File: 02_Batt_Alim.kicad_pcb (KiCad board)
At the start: 2 copper layers, 58.4 x 26.7 mm, 52 parts, among them IC1 TP4056, IC2 DW01A, J1 Conn_01x01, J10 Conn_01x01, J11 Conn_01x01, J12 Conn_01x01, J2 Conn_01x01, J3 Conn_01x01, J4 Conn_01x01, J5 Conn_01x01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

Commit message: routage
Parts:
- moved J3 55.8 mm to (104.1, 94.0), turned to 180 degrees
- moved J4 53.4 mm to (104.1, 91.4), turned to 180 degrees
- moved J5 51.4 mm to (104.1, 88.9), turned to 180 degrees
- moved J6 49.9 mm to (104.1, 86.4), turned to 180 degrees
- moved J7 48.9 mm to (104.1, 83.8), turned to 180 degrees
- moved J8 48.3 mm to (104.1, 81.3), turned to 180 degrees
- moved C3 46.5 mm to (108.0, 92.1), turned to 90 degrees
- moved R1 43.3 mm to (107.3, 87.6), turned to 90 degrees
- moved D5 41.4 mm to (113.0, 90.8), turned to 0 degrees
- moved U1 41.3 mm to (113.0, 94.0), turned to 180 degrees
- moved Q2 39.8 mm to (109.9, 87.0), turned to 180 degrees
- moved R15 38.4 mm to (130.8, 94.0)
- moved D6 37.1 mm to (127.2, 94.0), turned to 180 degrees
- moved R5 36.5 mm to (113.2, 86.4), turned to 180 degrees
- moved R2 35.2 mm to (113.2, 88.3), turned to 0 degrees
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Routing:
- net V_OUT: track 69.9 -> 35.5 mm
- net SWITCH_OUT: track 54.0 -> 27.5 mm, vias 0 -> 1
- net uC_2_V: track 34.4 -> 10.5 mm, vias 1 -> 0
- net GND: track 215.9 -> 235.8 mm, vias 31 -> 30
- net Net-(Q1-Pad4): track 4.02 -> 21.5 mm, vias 0 -> 2
- net 5V: track 19.6 -> 36.9 mm, vias 0 -> 2
- net V_BAT-: track 31.1 -> 25.0 mm, vias 1 -> 2
- net /LX: track 14.2 -> 18.1 mm
- net V_BAT+: track 46.6 -> 43.5 mm
- net V_2_uC: track 13.3 -> 10.4 mm
- net SWITCH_IN: track 67.7 -> 70.1 mm, vias 0 -> 2
- net /V_BAT+_F: track 7.08 -> 4.73 mm
- net Net-(IC2-Pad2): track 2.23 -> 3.87 mm
- net Net-(IC2-Pad1): track 11.4 -> 10.0 mm
- net Net-(IC2-Pad3): track 12.7 -> 11.5 mm, vias 2 -> 0
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- added copper zone on B.Cu, net V_BAT-
- removed copper zone on F.Cu, net /V_BAT+_F
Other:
- board size 58.4 x 26.7 mm -> 34.3 x 43.2 mm
- board text added: "Batt_Alim 2020/12/22"
- board text added: "https://github.com/ThierryOrlandi/02_Batt_Alim"
- board text removed: "Batt_Alim 2020/12/15"

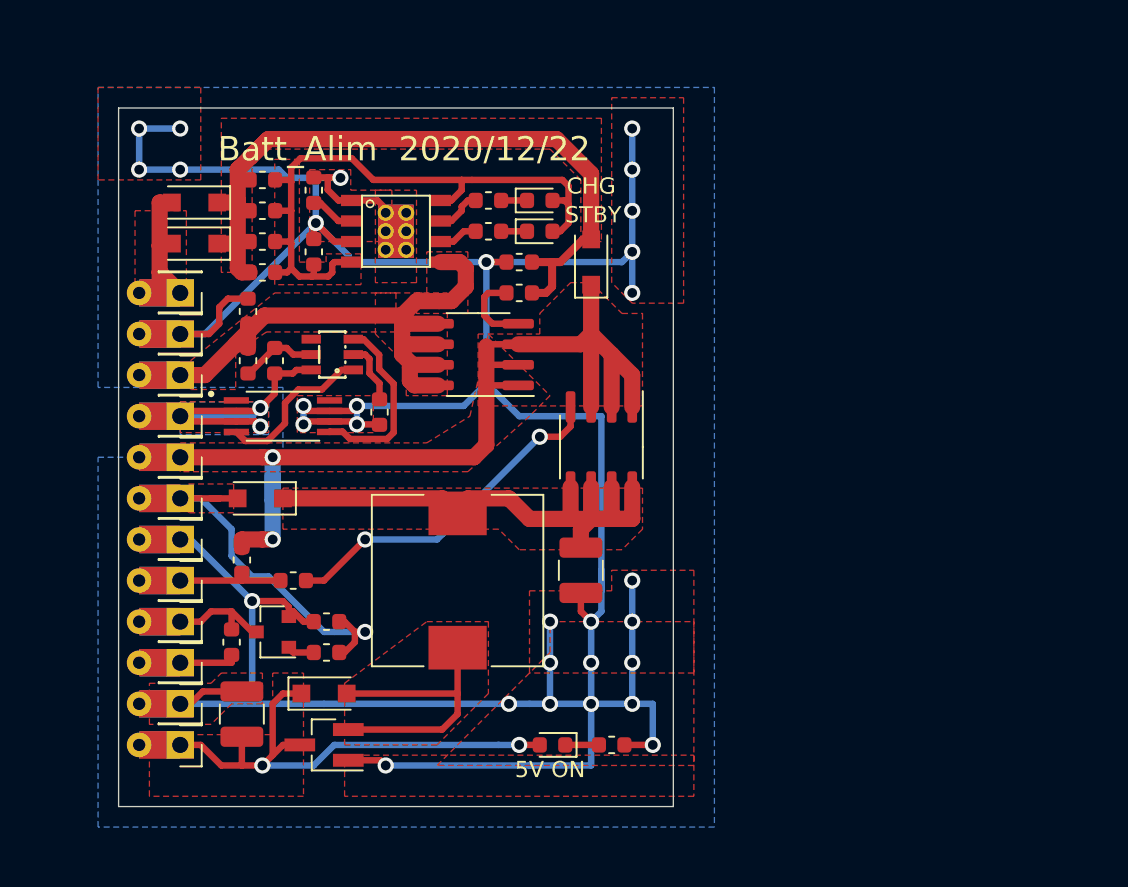
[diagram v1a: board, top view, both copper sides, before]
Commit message: simplify!
1) battery lipo protection deleted
2) move to schottky diodes instead of pmos for avoiding perturbation of charge while switch is on.
3) reduced size of pcb
4) added nmos for "hold" function
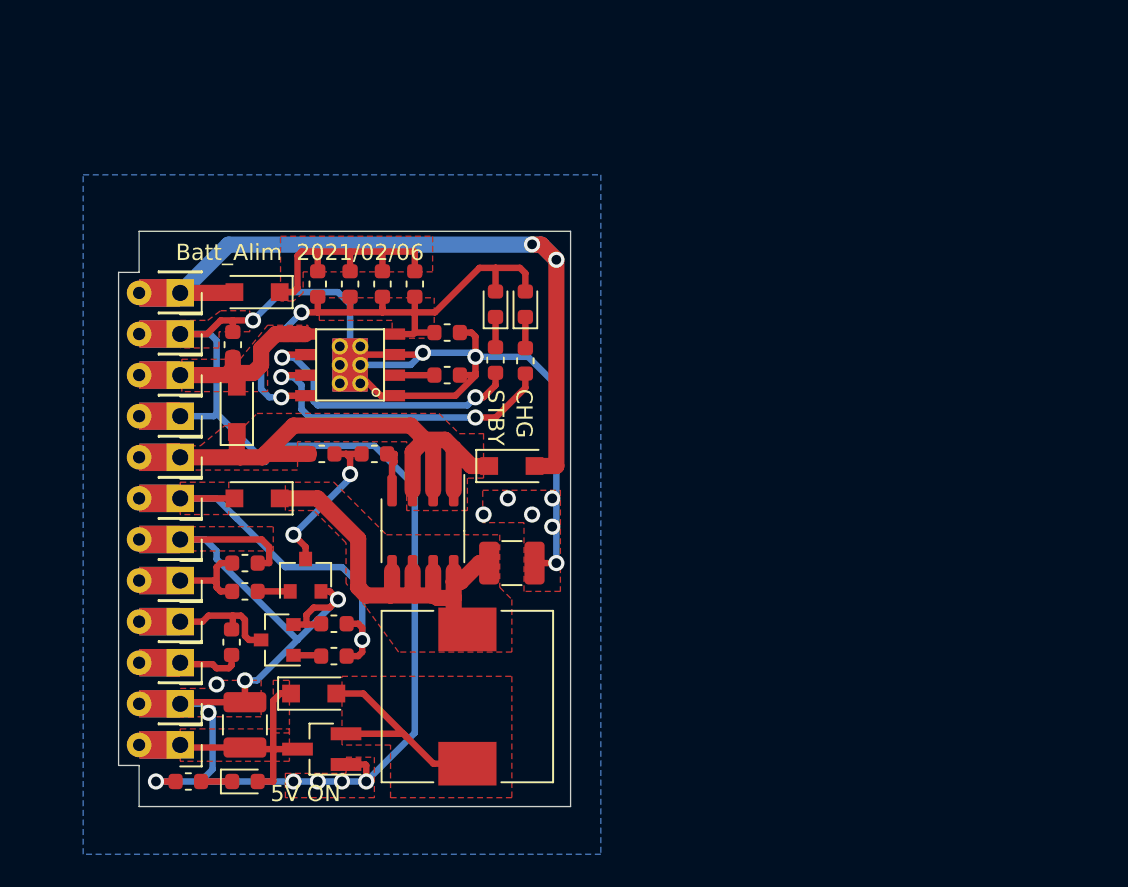
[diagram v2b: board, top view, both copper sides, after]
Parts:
- removed C5: 100nF, Capacitor_SMD:C_0603_1608Metric
- removed IC2: DW01A, Chimere:SOT23-6
- removed Q4: FS8205A, Chimere:SOP65P640X120-8N
- removed R16: 100, Resistor_SMD:R_0603_1608Metric
- removed R17: 1k, Resistor_SMD:R_0603_1608Metric
- removed REF**: OSHW-Symbol_6.7x6mm_SilkScreen, Symbol:OSHW-Symbol_6.7x6mm_SilkScreen
- removed REF**: KiCad-Logo2_5mm_SilkScreen, Symbol:KiCad-Logo2_5mm_SilkScreen
- Q3: value AO4407A -> 2N7002; footprint Package_SO:SOIC-8_3.9x4.9mm_P1.27mm -> Package_TO_SOT_SMD:SOT-23
- R11: value 100 -> 100K
- R13: value 100K -> 100
- R7: value 1k2 -> 10k
- moved R13 26.5 mm to (108.1, 84.5), turned to 0 degrees
- moved R15 26.3 mm to (104.6, 96.2), turned to 180 degrees
- moved R11 23.8 mm to (108.1, 82.7), turned to 0 degrees
- moved D6 19.1 mm to (108.1, 96.2), turned to 0 degrees
- moved Q3 17.3 mm to (111.9, 83.5), turned to 90 degrees
- moved R7 14.1 mm to (120.6, 71.1), turned to 0 degrees
- moved D4 13.5 mm to (124.6, 76.7), turned to 0 degrees
- moved Q1 12.2 mm to (119.1, 80.7)
- moved R9 11.4 mm to (118.6, 65.5), turned to 90 degrees
- moved D8 10.6 mm to (107.6, 73.2), turned to 90 degrees
- moved R6 10.2 mm to (125.5, 70.2), turned to 270 degrees
- moved C1 9.64 mm to (120.6, 68.5), turned to 0 degrees
- moved R4 9.30 mm to (116.1, 76.0)
- moved IC1 8.73 mm to (114.6, 70.5), turned to 180 degrees
- moved R10 8.69 mm to (116.6, 65.5), turned to 90 degrees
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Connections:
- D4 pad 2: V_ext_p -> V_ext
- D7 pad 1: V_ext_p -> /V_ext_p
- D8 pad 1: V_ext_p -> SWITCH_IN
- D8 pad 2: V_ext -> V_BAT+
- J10 pad 1: V_BAT- -> GND
- Q3 pad 1: SWITCH_IN -> Net-(Q3-Pad1)
- Q3 pad 2: SWITCH_IN -> GND
- Q3 pad 3: SWITCH_IN -> Net-(Q3-Pad3)
- R10 pad 2: V_ext_p -> /V_ext_p
- R11 pad 1: V_ext_p -> uC_2_V
- R11 pad 2: Net-(Q3-Pad4) -> GND
- R12 pad 2: V_ext_p -> /V_ext_p
- R13 pad 1: V_ext_p -> uC_2_V
- R13 pad 2: GND -> Net-(Q3-Pad1)
- R14 pad 2: V_ext_p -> /V_ext_p
- R3 pad 2: uC_2_V -> Net-(Q3-Pad3)
- R4 pad 1: uC_2_V -> Net-(Q3-Pad3)
- R9 pad 2: V_ext_p -> /V_ext_p
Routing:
- net V_ext_p: track 56.5 -> 0.00 mm
- net GND: track 235.8 -> 182.3 mm, vias 30 -> 18
- net V_ext: track 14.0 -> 50.6 mm, vias 0 -> 2
- net SWITCH_IN: track 70.1 -> 38.8 mm, vias 2 -> 0
- net V_BAT+: track 43.5 -> 15.0 mm
- net V_BAT-: track 25.0 -> 0.00 mm, vias 2 -> 0
- net 5V: track 36.9 -> 17.1 mm, vias 2 -> 0
- net Net-(Q1-Pad4): track 21.5 -> 2.80 mm, vias 2 -> 0
- net Net-(IC1-Pad7): track 2.85 -> 20.7 mm, vias 0 -> 2
- net Net-(IC1-Pad6): track 2.44 -> 18.1 mm, vias 0 -> 2
- net /V_ext_p: track 0.00 -> 15.5 mm
- net Net-(IC2-Pad3): track 11.5 -> 0.00 mm
- net Net-(Q3-Pad3): track 0.00 -> 10.0 mm, vias 0 -> 2
- net Net-(IC2-Pad1): track 10.0 -> 0.00 mm
- net V_OUT: track 35.5 -> 26.4 mm
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- added copper zone on F.Cu, net /V_ext_p
- removed copper zone on B.Cu, net V_BAT-
- removed copper zone on F.Cu, net V_BAT-
- removed copper zone on F.Cu, net V_ext
- removed copper zone on F.Cu, net V_ext_p
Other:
- board size 34.3 x 43.2 mm -> 27.9 x 35.6 mm
- board text added: "BAT+"
- board text added: "Batt_Alim 2021/02/06"
- board text added: "github.com/ ThierryOrlandi/ 02_Batt_Alim"
- board text removed: "-BAT+"
- board text removed: "Batt_Alim 2020/12/22"
- board text removed: "https://github.com/ThierryOrlandi/02_Batt_Alim"

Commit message: simplification
simplified the whole design
Gerbers generated
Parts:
- removed D1: 1N5819W, Diode_SMD:D_SOD-123F
- removed J10, J11, J12, J4, J5, J6, J7, J8: Conn_01x01, Chimere:Castellated_conn
- removed Q1: AO4407A, Package_SO:SOIC-8_3.9x4.9mm_P1.27mm
- removed Q2, Q3: 2N7002, Package_TO_SOT_SMD:SOT-23
- removed R1, R11, R3, R5: 100K, Resistor_SMD:R_0603_1608Metric
- removed R13, R2, R4: 100, Resistor_SMD:R_0603_1608Metric
- added REF**: OSHW-Logo2_7.3x6mm_SilkScreen, Symbol:OSHW-Logo2_7.3x6mm_SilkScreen, B.Cu at (121.8, 65.6)
- added REF**: KiCad-Logo2_5mm_SilkScreen, Symbol:KiCad-Logo2_5mm_SilkScreen, B.Cu at (116.6, 76.9)
- moved J3 20.3 mm to (104.1, 73.7)
- moved C4 17.2 mm to (108.3, 77.1), turned to 180 degrees
- moved D6 13.2 mm to (105.8, 83.2), turned to 90 degrees
- moved R15 11.5 mm to (103.8, 84.7), turned to 270 degrees
- moved U1 10.9 mm to (111.9, 83.3), turned to 90 degrees
- moved L1 10.7 mm to (121.9, 80.3)
- moved D4 9.68 mm to (126.9, 67.3), turned to 90 degrees
- moved C3 9.00 mm to (108.4, 83.7), turned to 270 degrees
- moved D5 7.45 mm to (115.0, 83.8), turned to 270 degrees
- moved R8 1.34 mm to (123.0, 69.0)
- moved D2 1.34 mm to (124.9, 65.5)
- moved D3 1.34 mm to (123.0, 65.5)
- moved R6 1.34 mm to (124.9, 69.0)
- moved D8 1.28 mm to (108.4, 74.2), turned to 180 degrees
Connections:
- C4 pad 1: V_OUT -> V_sum
- D4 pad 1: SWITCH_IN -> V_sum
- D8 pad 1: SWITCH_IN -> V_sum
- L1 pad 2: V_OUT -> V_sum
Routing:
- net GND: track 182.3 -> 70.7 mm, vias 18 -> 13
- net SWITCH_IN: track 38.8 -> 0.00 mm
- net SWITCH_OUT: track 27.9 -> 0.00 mm, vias 1 -> 0
- net V_sum: track 0.00 -> 27.5 mm
- net V_OUT: track 26.4 -> 0.00 mm
- net V_ext: track 50.6 -> 38.8 mm
- net V_2_uC: track 11.1 -> 0.00 mm
- net Net-(Q3-Pad3): track 10.0 -> 0.00 mm, vias 2 -> 0
- net uC_2_V: track 9.51 -> 0.00 mm
- net V_uC: track 7.85 -> 0.00 mm
- net V_BAT+: track 15.0 -> 18.1 mm
- net Net-(Q1-Pad4): track 2.80 -> 0.00 mm
- net V_chg: track 34.1 -> 31.3 mm
- net Net-(Q3-Pad1): track 2.01 -> 0.00 mm
- net Net-(Q2-Pad1): track 1.73 -> 0.00 mm
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- added copper zone on F.Cu, net V_sum
- removed copper zone on F.Cu, net SWITCH_IN
- removed copper zone on F.Cu, net SWITCH_OUT
- removed copper zone on F.Cu, net V_OUT
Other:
- board size 27.9 x 35.6 mm -> 29.2 x 25.4 mm
- board text added: "Batt_Alim 2021/02/23"
- board text removed: "Batt_Alim 2021/02/06"
- board text removed: "SW_IN"
- board text removed: "SW_OUT"
- board text removed: "V2uC"
- board text removed: "VuC"
- board text removed: "uC2V"
